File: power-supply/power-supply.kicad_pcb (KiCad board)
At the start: 2 copper layers, 70 x 130 mm, 34 parts, among them J1 Barrel_Jack, J2 Output, J3 Output, SW1 SW_SPDT, U1 L7812, U2 L7912, U3 L7805

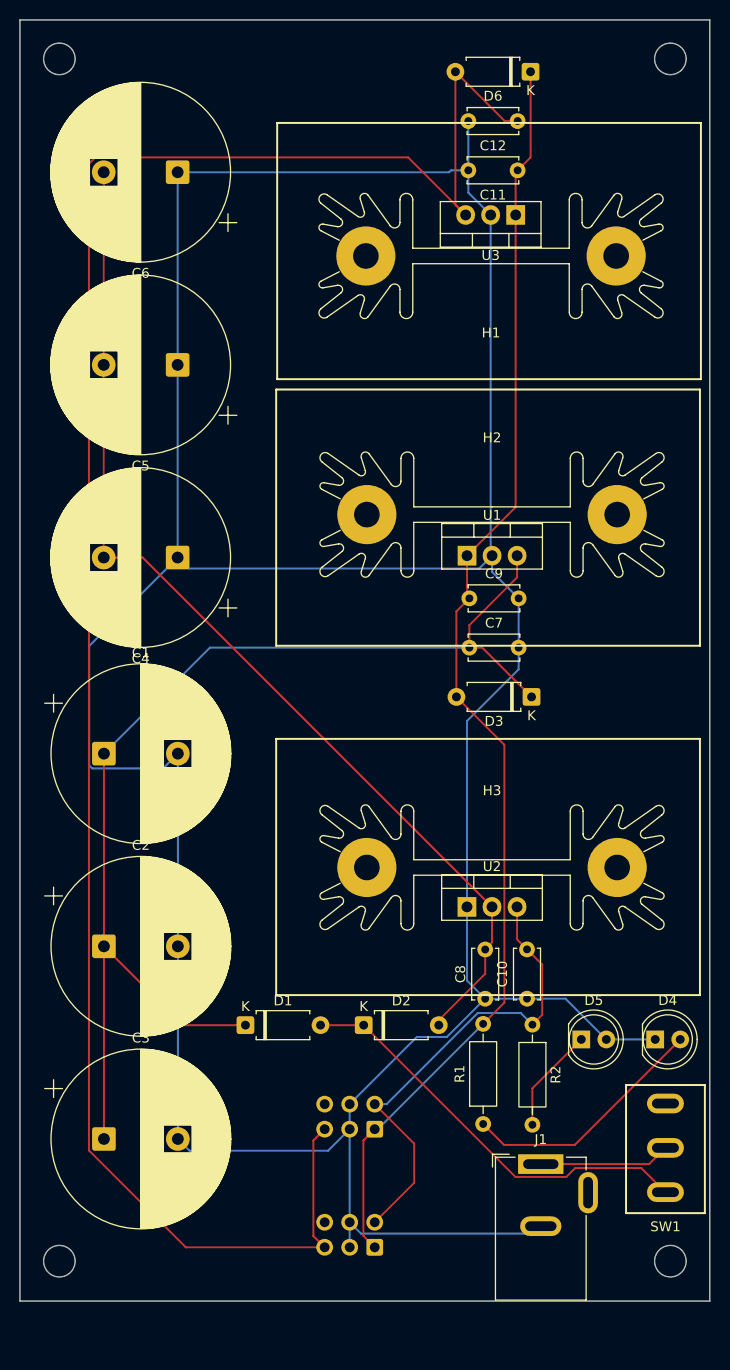
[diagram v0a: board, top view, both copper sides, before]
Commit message: First pass of power supply
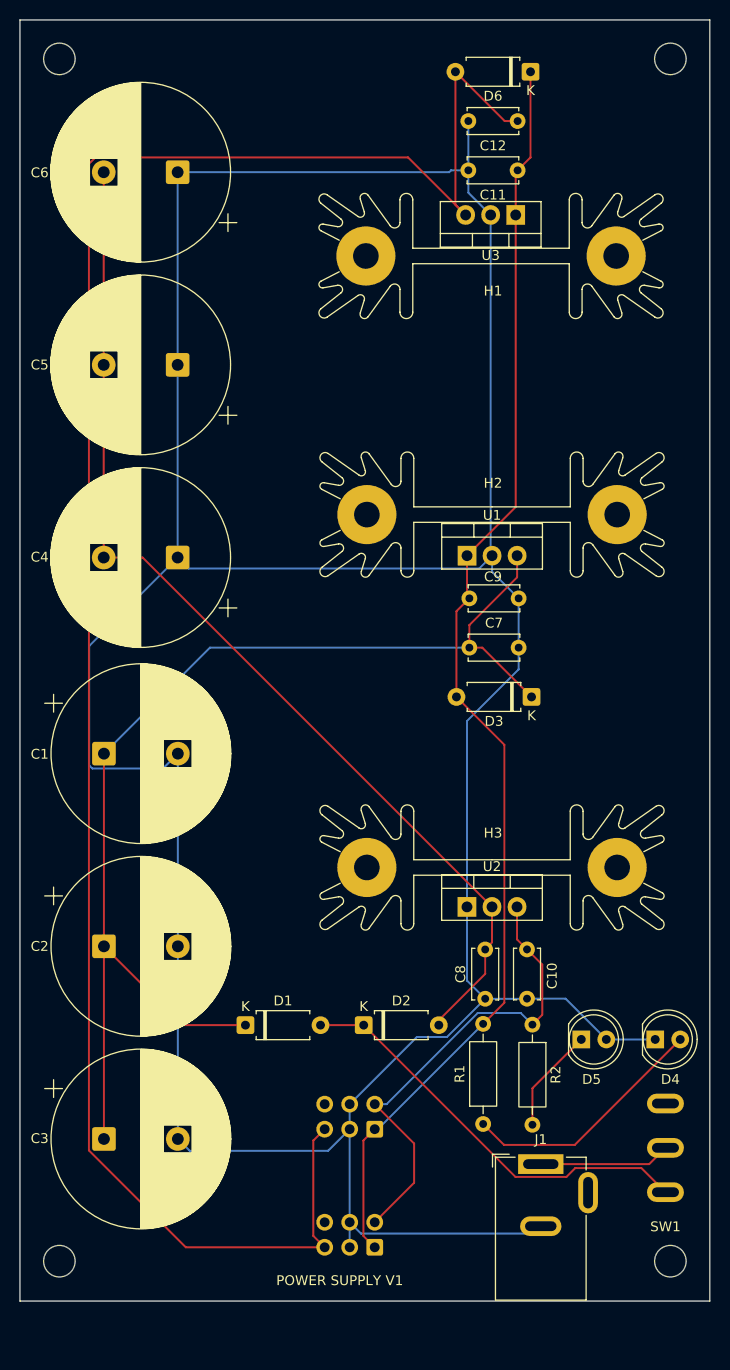
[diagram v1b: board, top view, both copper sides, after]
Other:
- board text added: "POWER SUPPLY V1"
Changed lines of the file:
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@@
 		(tags "heatsink")
 		(property "Reference" "H3"
-			(at 0 -7.8 0)
+			(at 0.100142 -3.499778 0)
 			(layer "F.SilkS")
 			(effects
@@
 			(layer "F.SilkS")
 		)
-		(fp_line
-			(start -18 -7)
-			(end -18 7)
-			(stroke
-				(width 0.05)
-				(type solid)
-			)
-			(layer "F.CrtYd")
-		)
-		(fp_line
-			(start -18 -7)
-			(end 18 -7)
-			(stroke
-				(width 0.05)
-				(type solid)
-			)
-			(layer "F.CrtYd")
-		)
-		(fp_line
-			(start 18 7)
-			(end -18 7)
-			(stroke
-				(width 0.05)
-				(type solid)
-			)
-			(layer "F.CrtYd")
-		)
-		(fp_line
-			(start 18 7)
-			(end 18 -7)
-			(stroke
-				(width 0.05)
-				(type solid)
-			)
-			(layer "F.CrtYd")
-		)
 		(fp_rect
 			(start -17.9 -6.9)
@@
 		(tags "LED")
 		(property "Reference" "D5"
-			(at 1.27 -3.96 0)
+			(at 1.04 4.05 0)
 			(layer "F.SilkS")
 			(effects
@@
 		(tags "C Disc series Radial pin pitch 5.00mm diameter 5mm width 2.5mm Capacitor")
 		(property "Reference" "C9"
-			(at 2.5 -2.5 0)
+			(at 2.397892 -2.191883 0)
 			(layer "F.SilkS")
 			(effects
@@
 		(tags "CP Radial series Radial pin pitch 7.50mm diameter 18mm height 35mm Electrolytic Capacitor")
 		(property "Reference" "C3"
-			(at 3.75 -10.25 0)
+			(at -6.52222 -0.05 0)
 			(layer "F.SilkS")
 			(effects
@@
 		(tags "LED")
 		(property "Reference" "D4"
-			(at 1.27 -3.96 0)
+			(at 1.54 4.05 0)
 			(layer "F.SilkS")
 			(effects
@@
 		(tags "heatsink")
 		(property "Reference" "H1"
-			(at 0 -7.8 0)
+			(at -0.2 -3.55 0)
 			(layer "F.SilkS")
 			(effects
@@
 			(layer "F.SilkS")
 		)
-		(fp_line
-			(start 18 7)
-			(end 18 -7)
-			(stroke
-				(width 0.05)
-				(type solid)
-			)
-			(layer "F.CrtYd")
-		)
-		(fp_line
-			(start 18 7)
-			(end -18 7)
-			(stroke
-				(width 0.05)
-				(type solid)
-			)
-			(layer "F.CrtYd")
-		)
-		(fp_line
-			(start -18 -7)
-			(end 18 -7)
-			(stroke
-				(width 0.05)
-				(type solid)
-			)
-			(layer "F.CrtYd")
-		)
-		(fp_line
-			(start -18 -7)
-			(end -18 7)
-			(stroke
-				(width 0.05)
-				(type solid)
-			)
-			(layer "F.CrtYd")
-		)
 		(fp_rect
 			(start -17.9 -6.9)
@@
 		(tags "CP Radial series Radial pin pitch 7.50mm diameter 18mm height 35mm Electrolytic Capacitor")
 		(property "Reference" "C2"
-			(at 3.75 -10.25 0)
+			(at -6.52222 0 0)
 			(layer "F.SilkS")
 			(effects
@@
 		(tags "CP Radial series Radial pin pitch 7.50mm diameter 18mm height 35mm Electrolytic Capacitor")
 		(property "Reference" "C5"
-			(at 3.75 -10.25 0)
+			(at 14 0 0)
 			(layer "F.SilkS")
 			(effects
@@
 		(tags "C Disc series Radial pin pitch 5.00mm diameter 5mm width 2.5mm Capacitor")
 		(property "Reference" "C10"
-			(at 2.5 -2.5 90)
+			(at 2.31345 2.546962 90)
 			(layer "F.SilkS")
 			(effects
@@
 		(tags "CP Radial series Radial pin pitch 7.50mm diameter 18mm height 35mm Electrolytic Capacitor")
 		(property "Reference" "C4"
-			(at 3.75 -10.25 0)
+			(at 14 0.05 0)
 			(layer "F.SilkS")
 			(effects
@@
 		(tags "heatsink")
 		(property "Reference" "H2"
-			(at 0 -7.8 0)
+			(at 0.097892 -3.191883 0)
 			(layer "F.SilkS")
 			(effects
@@
 			(layer "F.SilkS")
 		)
-		(fp_line
-			(start -18 -7)
-			(end -18 7)
-			(stroke
-				(width 0.05)
-				(type solid)
-			)
-			(layer "F.CrtYd")
-		)
-		(fp_line
-			(start -18 -7)
-			(end 18 -7)
-			(stroke
-				(width 0.05)
-				(type solid)
-			)
-			(layer "F.CrtYd")
-		)
-		(fp_line
-			(start 18 7)
-			(end -18 7)
-			(stroke
-				(width 0.05)
-				(type solid)
-			)
-			(layer "F.CrtYd")
-		)
-		(fp_line
-			(start 18 7)
-			(end 18 -7)
-			(stroke
-				(width 0.05)
-				(type solid)
-			)
-			(layer "F.CrtYd")
-		)
 		(fp_rect
 			(start -17.9 -6.9)
@@
 		(tags "CP Radial series Radial pin pitch 7.50mm diameter 18mm height 35mm Electrolytic Capacitor")
 		(property "Reference" "C6"
-			(at 3.75 -10.25 0)
+			(at 14 -0.05 0)
 			(layer "F.SilkS")
 			(effects
@@
 		(tags "CP Radial series Radial pin pitch 7.50mm diameter 18mm height 35mm Electrolytic Capacitor")
 		(property "Reference" "C1"
-			(at 3.75 -10.25 0)
+			(at -6.52222 0.05 0)
 			(layer "F.SilkS")
 			(effects
@@
 		)
 		(fill no)
-		(layer "F.SilkS")
+		(layer "Dwgs.User")
 	)
 	(gr_rect
@@
 		)
 		(fill no)
-		(layer "F.SilkS")
+		(layer "Dwgs.User")
 	)
 	(gr_rect
@@
 		)
 		(fill no)
-		(layer "F.SilkS")
+		(layer "Dwgs.User")
 	)
 	(gr_rect
@@
 		)
 		(fill no)
-		(layer "F.SilkS")
+		(layer "Dwgs.User")
 	)
 	(gr_rect
@@
 		(layer "Edge.Cuts")
 	)
+	(gr_text "POWER SUPPLY V1"
+		(at 89 166 0)
+		(layer "F.SilkS")
+		(effects
+			(font
+				(size 1 1)
+				(thickness 0.1)
+			)
+			(justify left bottom)
+		)
+	)
 	(segment

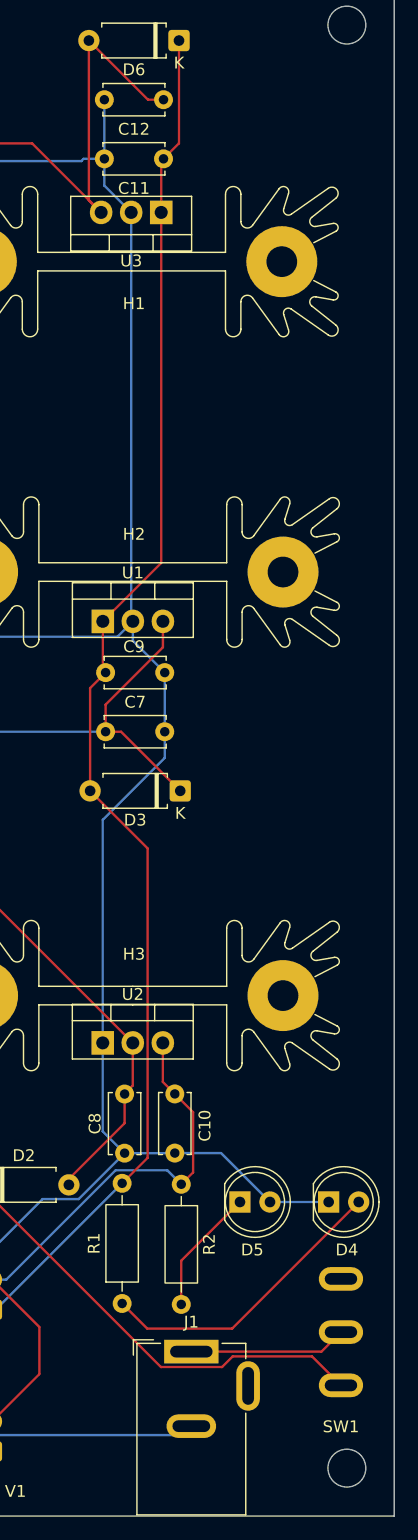
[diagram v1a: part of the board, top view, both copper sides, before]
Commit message: Update power supply
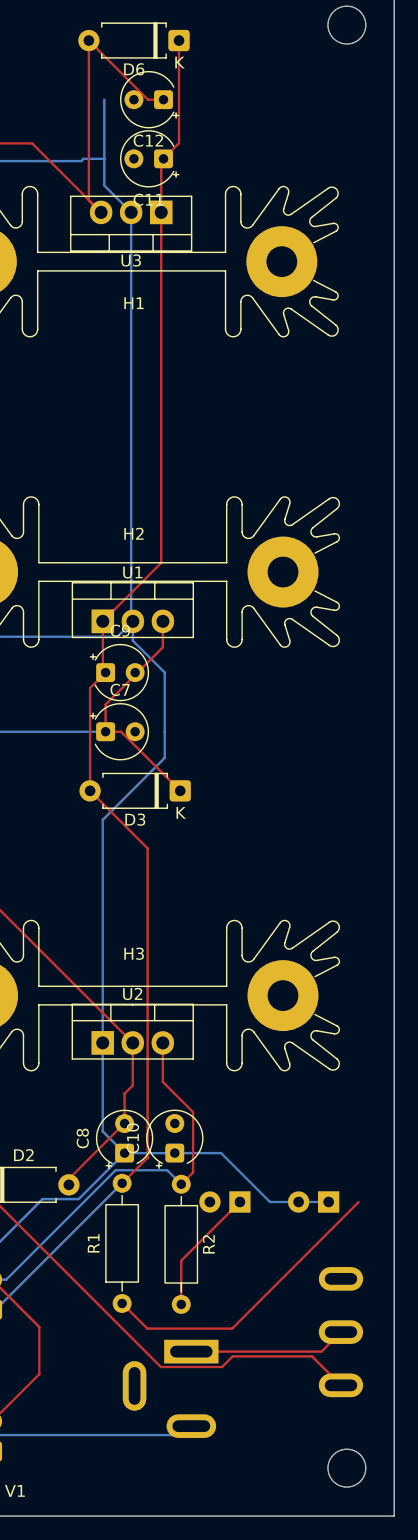
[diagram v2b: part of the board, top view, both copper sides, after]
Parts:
- C10, C11, C12, C7, C8, C9: footprint Capacitor_THT:C_Disc_D5.0mm_W2.5mm_P5.00mm -> Capacitor_THT:CP_Radial_Tantal_D4.5mm_P2.50mm
- D4, D5, J1, SW1: moved to B.Cu
- turned D4 to 180 degrees
- turned D5 to 180 degrees
- turned J1 to 180 degrees
- turned SW1 to 180 degrees

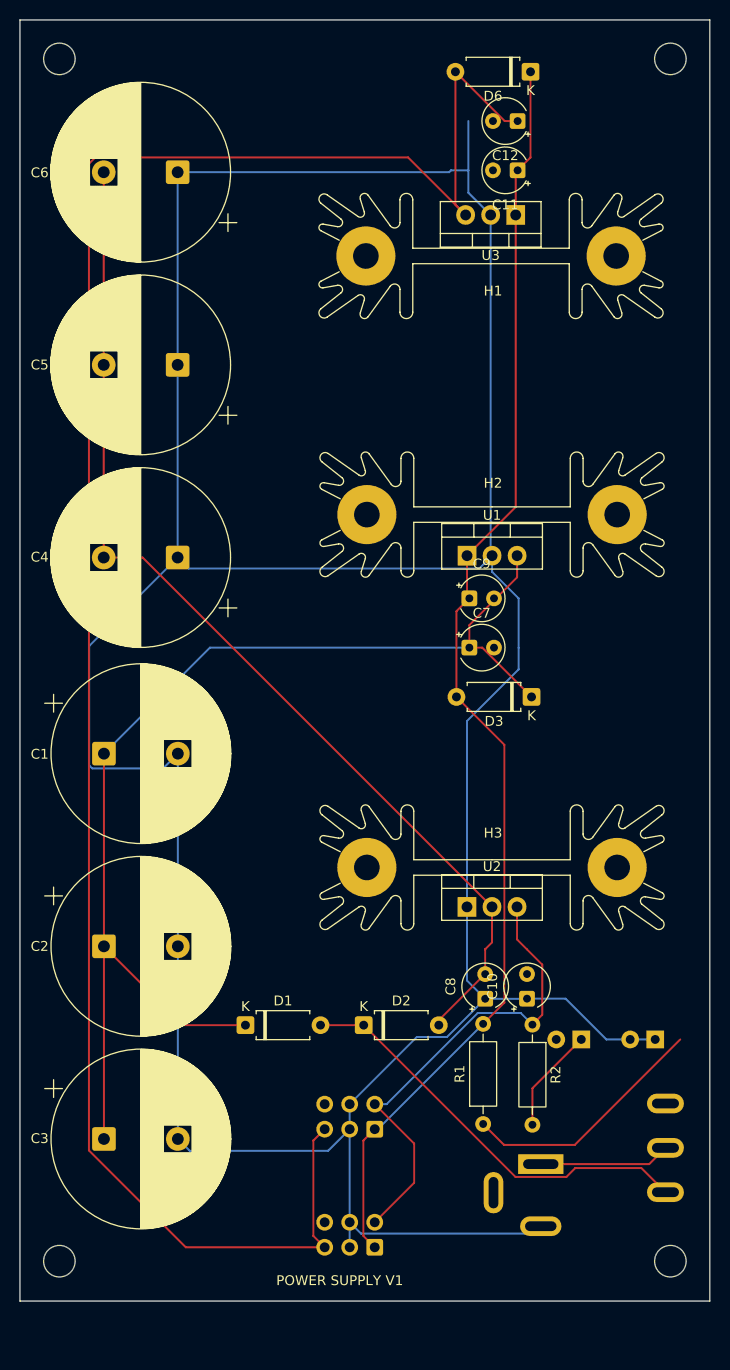
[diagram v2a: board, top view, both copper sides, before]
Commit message: Fix L812 orientation in power supply
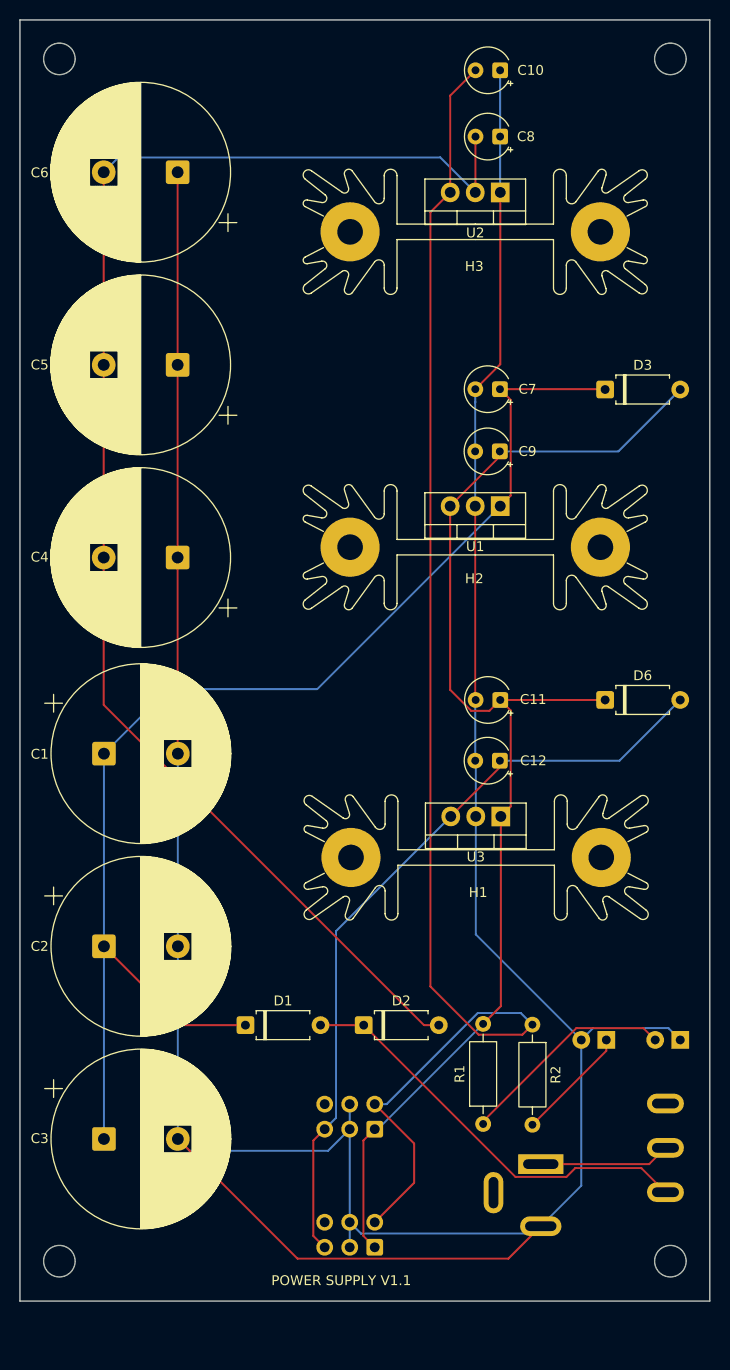
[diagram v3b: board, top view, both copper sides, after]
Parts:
- U1: value L7812 -> LM7812_TO220
- moved C10 94.2 mm to (111.7, 42.6), turned to 180 degrees
- moved C8 87.5 mm to (111.7, 49.3), turned to 180 degrees
- moved U2 72.6 mm to (111.7, 55.0), turned to 180 degrees
- moved C12 64.9 mm to (111.7, 112.7)
- moved H3 64.5 mm to (109.2, 59.0), turned to 180 degrees
- moved D6 64.2 mm to (122.4, 106.5), turned to 0 degrees
- moved U3 61.1 mm to (111.8, 118.3)
- moved H1 61.1 mm to (109.3, 122.5)
- moved C11 53.8 mm to (111.7, 106.5)
- moved D3 32.1 mm to (122.4, 75.0), turned to 0 degrees
- moved C7 26.4 mm to (111.7, 75.0), turned to 180 degrees
- moved C9 15.2 mm to (111.7, 81.3), turned to 180 degrees
- moved U1 6.05 mm to (111.7, 86.8), turned to 180 degrees
- moved H2 3.72 mm to (109.2, 91.0), turned to 180 degrees
- moved D4 2.54 mm to (130.0, 141.0)
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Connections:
- U1 pad 1: Net-(D3-A) -> Net-(D1-K)
- U1 pad 3: Net-(D1-K) -> Net-(D3-A)
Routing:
- net Net-(D6-A): track 205.3 -> 78.5 mm
- net Net-(J2-Pin_2): track 49.0 -> 143.3 mm
- net Net-(D2-A): track 107.4 -> 147.5 mm
- net GND: track 360.6 -> 331.4 mm
- net Net-(D1-K): track 118.0 -> 131.7 mm
- net Net-(D3-A): track 132.0 -> 127.1 mm
- net Net-(D4-A): track 25.3 -> 22.1 mm
- net Net-(D5-K): track 10.7 -> 11.7 mm
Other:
- board text added: "POWER SUPPLY V1.1"
- board text removed: "POWER SUPPLY V1"

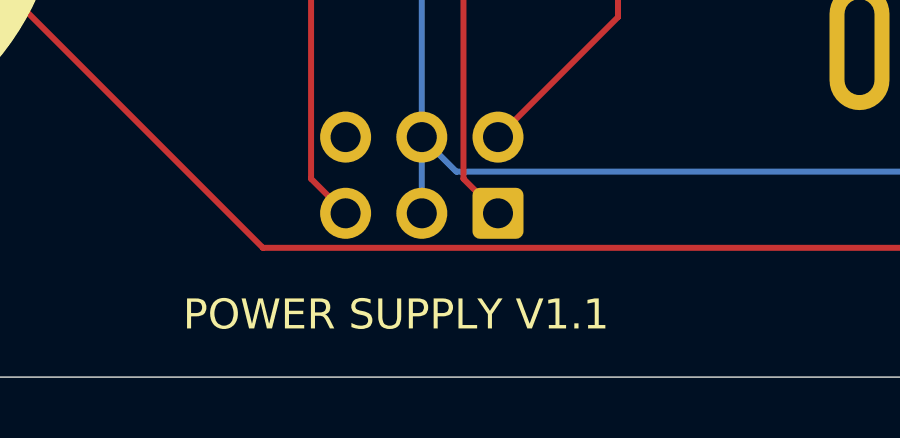
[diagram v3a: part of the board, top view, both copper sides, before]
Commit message: Redesign oscillator
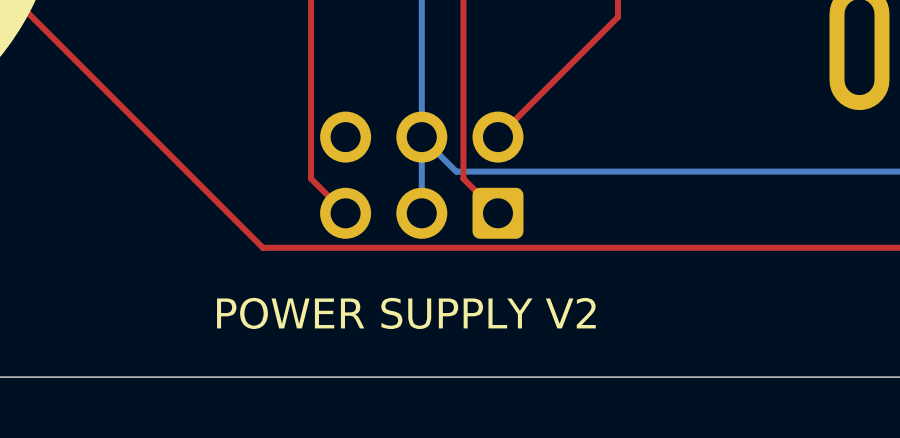
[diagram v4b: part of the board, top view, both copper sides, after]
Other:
- board text added: "POWER SUPPLY V2"
- board text removed: "POWER SUPPLY V1.1"
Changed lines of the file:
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@@
 		(layer "Edge.Cuts")
 	)
-	(gr_text "POWER SUPPLY V1.1"
-		(at 88.5 166 0)
+	(gr_text "POWER SUPPLY V2"
+		(at 89.5 166 0)
 		(layer "F.SilkS")
 		(effects
